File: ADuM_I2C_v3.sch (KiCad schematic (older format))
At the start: 42 parts, among them J1 A, J2 B, Q1 BSS138, Q2 BSS138, Q3 BSS138, Q4 BSS138, Q5 BSS138, Q6 BSS138, Q7 BSS138, Q8 BSS138, U1 ADuM1251ARZ, U2 ADuM1201AR

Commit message: Сформирован перечень элементов, 3D-модель, исправлены ошибки, реализована панелизация платы.
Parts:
- J1, J2: footprint Connector_PinHeader_1.27mm:PinHeader_2x03_P1.27mm_Horizontal -> Modules:PinHeader_2x03_P1.27mm_Horizontal_short
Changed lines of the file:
@@
 F 0 "J2" H 5125 4550 50  0000 C CNN
 F 1 "B" H 5125 4950 50  0000 C CNN
-F 2 "Connector_PinHeader_1.27mm:PinHeader_2x03_P1.27mm_Horizontal" H 5075 4750 50  0001 C CNN
+F 2 "Modules:PinHeader_2x03_P1.27mm_Horizontal_short" H 5075 4750 50  0001 C CNN
 F 3 "~" H 5075 4750 50  0001 C CNN
 	1    5075 4750
@@
 F 0 "J1" H 2875 4950 50  0000 C CNN
 F 1 "A" H 2875 4550 50  0000 C CNN
-F 2 "Connector_PinHeader_1.27mm:PinHeader_2x03_P1.27mm_Horizontal" H 2825 4750 50  0001 C CNN
+F 2 "Modules:PinHeader_2x03_P1.27mm_Horizontal_short" H 2825 4750 50  0001 C CNN
 F 3 "~" H 2825 4750 50  0001 C CNN
 	1    2825 4750

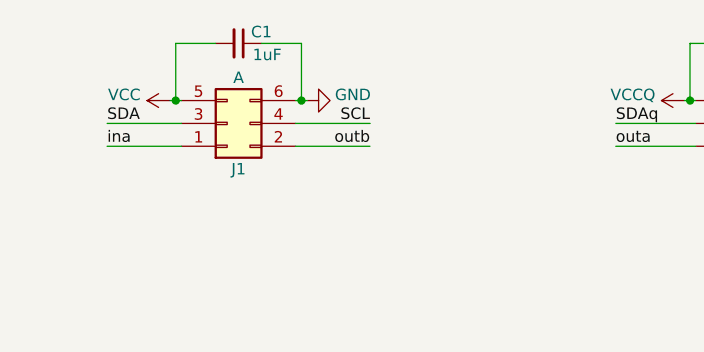
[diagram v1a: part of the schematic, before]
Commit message: Добавил изолирующие отверстия на схему. Подправил компоненты отверстий. Удалил контуры отверстий на обеих слоях платы. Обновил гербера и 3D-модель (step-файл).
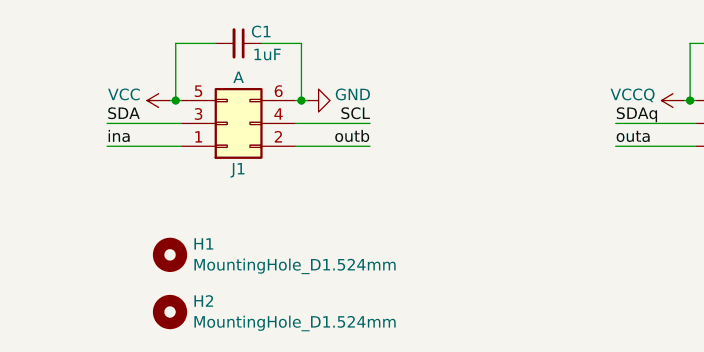
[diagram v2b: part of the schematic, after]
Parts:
- added H1, H2: MountingHole_D1.524mm, Modules:MountingHole_D1.524mm, symbol Mechanical:MountingHole
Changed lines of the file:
@@
 	1    0    0    1
 $EndComp
+$Comp
+L Mechanical:MountingHole H1
+U 1 1 61FB05C8
+P 2575 5325
+F 0 "H1" H 2675 5371 50  0000 L CNN
+F 1 "MountingHole_D1.524mm" H 2675 5280 50  0000 L CNN
+F 2 "Modules:MountingHole_D1.524mm" H 2575 5325 50  0001 C CNN
+F 3 "~" H 2575 5325 50  0001 C CNN
+	1    2575 5325
+	1    0    0    -1
+$EndComp
+$Comp
+L Mechanical:MountingHole H2
+U 1 1 61FB1324
+P 2575 5575
+F 0 "H2" H 2675 5621 50  0000 L CNN
+F 1 "MountingHole_D1.524mm" H 2675 5530 50  0000 L CNN
+F 2 "Modules:MountingHole_D1.524mm" H 2575 5575 50  0001 C CNN
+F 3 "~" H 2575 5575 50  0001 C CNN
+	1    2575 5575
+	1    0    0    -1
+$EndComp
 $EndSCHEMATC
